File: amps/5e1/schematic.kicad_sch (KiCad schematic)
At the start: 26 parts, among them T1 SE 5k:8

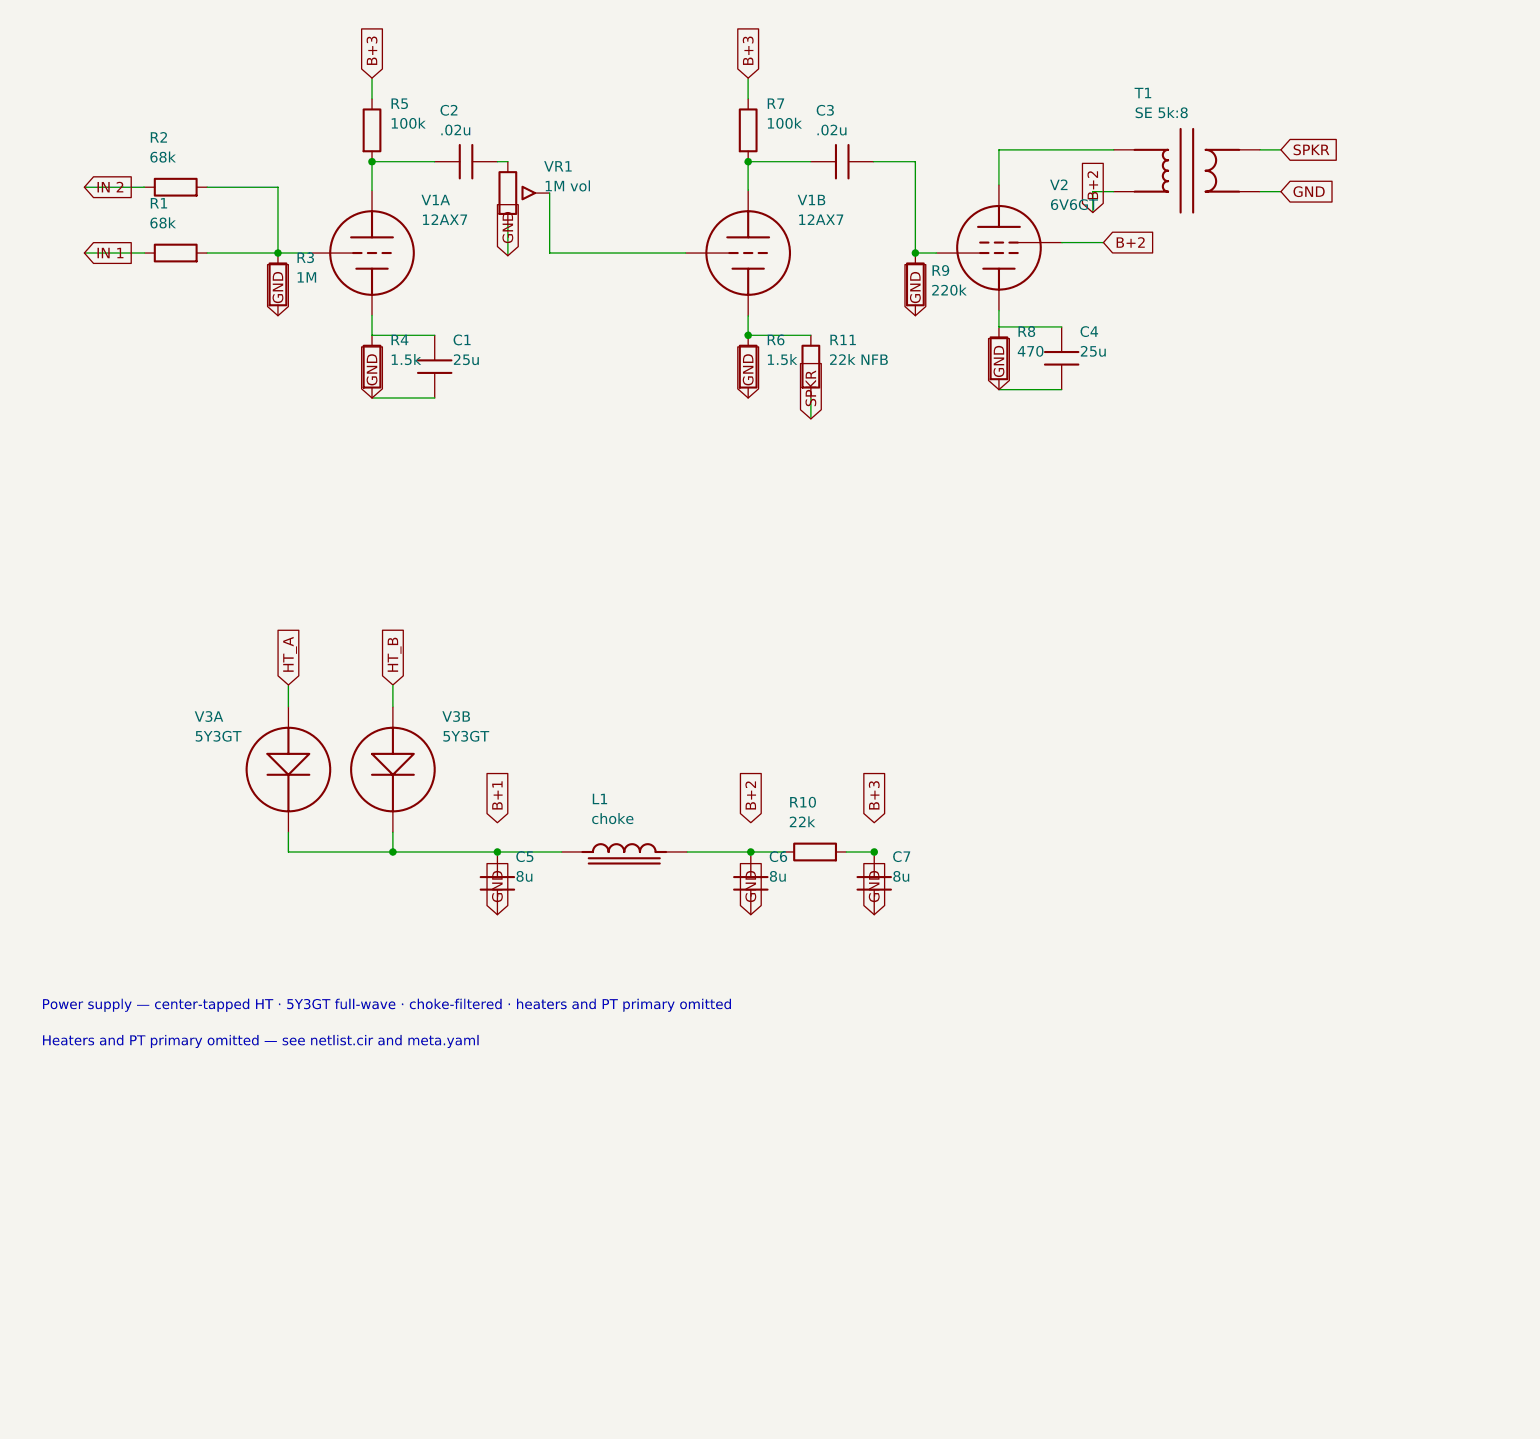
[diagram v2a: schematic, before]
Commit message: Fix: rotated global labels lettered their net names outside the flag
Every global label this pipeline emitted carried (justify left) regardless of
rotation. KiCanvas — like KiCad — draws label text horizontally at 0/180 and
vertically at 90/270 and reads WHICH SIDE of the anchor it letters on from the
justification, so at 180 and 270 the name printed outside an empty flag
outline, struck through by the very wire it names: 219 labels at 180 deg
(including the input-jack flags at top-left of nearly every sheet, the first
glyphs a visitor reads) and 792 GND/rail flags at 270 whose names squeezed at
the flag mouth instead of lettering down the body. The library already
compensated rotation for property text (`pa`); this mirrors that logic for
global labels: justify right at 180/270, left at 0/90.

check_schematics gains the geometry clause whose absence let all 1011
instances through a "no lettering through circuitry" pass: it modelled the
flag box but never the label TEXT, so a name rendered on the wrong side was
invisible to it. The gate now proves justification compensates rotation on
every global label.

Two more things this exposed, fixed in the same engine pass:

- Placement now measures with the renderer's own Newstroke advance table
  (extracted from the vendored kicanvas.js) instead of a flat 0.68-em prose
  average that under-read part lettering by a quarter — the mechanism behind
  every "metered clean, printed through its neighbour" incident. The GATE
  deliberately keeps the coarse ruler: re-ruling it with renderer truth was
  tried and red-flagged 28 of 34 sheets over abutments three visual passes
  had already judged sub-visual (the two-rulers note in schematic_lib.py).
- place_captions' escape ladder runs further, because a banner caption
  measured truly is half again wider than the old estimate believed.

All 34 schematics regenerated; full gate suite green.

🤖 Generated with [Claude Code](https://claude.com/claude-code)

Co-Authored-By: Claude Fable 5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
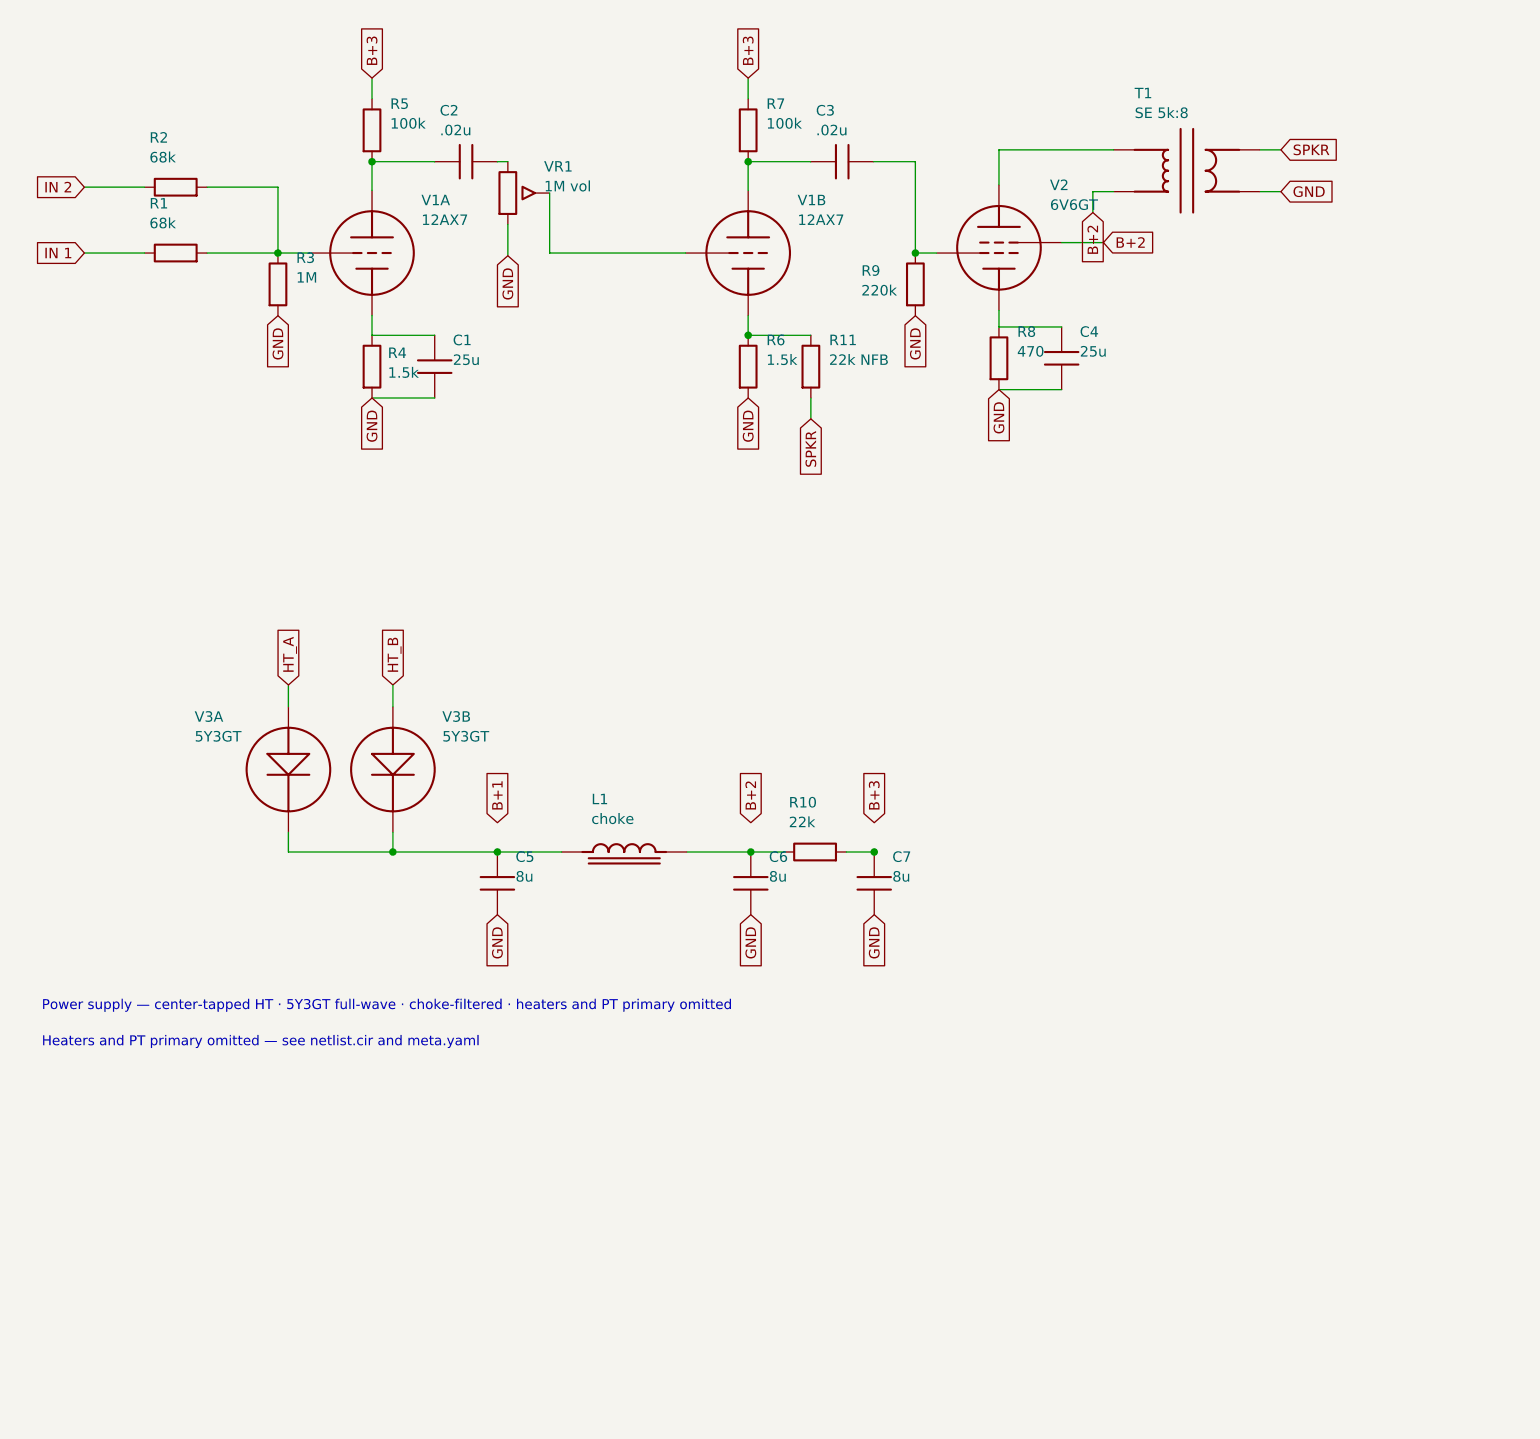
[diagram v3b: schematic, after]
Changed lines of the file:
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@@
     (comment 3 "Values read from: https://el34world.com/charts/Schematics/files/Fender/Fender_champ_5e1.pdf"))
   (global_label "IN 1" (shape input) (at 17.8816 38.278 180)
-    (effects (font (size 1.27 1.27)) (justify left)))
+    (effects (font (size 1.27 1.27)) (justify right)))
   (wire (pts (xy 17.8816 38.278) (xy 25.1716 38.278))
     (stroke (width 0) (type default)))
@@
     (stroke (width 0) (type default)))
   (global_label "IN 2" (shape input) (at 17.8816 30.278 180)
-    (effects (font (size 1.27 1.27)) (justify left)))
+    (effects (font (size 1.27 1.27)) (justify right)))
   (wire (pts (xy 17.8816 30.278) (xy 25.1716 30.278))
     (stroke (width 0) (type default)))
@@
     (property "Value" "1M" (at 43.6116 41.288 0) (effects (font (size 1.27 1.27)) (justify left))))
   (global_label "GND" (shape input) (at 41.4116 45.898 270)
-    (effects (font (size 1.27 1.27)) (justify left)))
+    (effects (font (size 1.27 1.27)) (justify right)))
   (wire (pts (xy 41.4116 38.278) (xy 45.2216 38.278))
     (stroke (width 0) (type default)))
@@
   (symbol (lib_id "cx:R") (at 52.8416 52.088 0) (unit 1)
     (in_bom yes) (on_board yes)
-    (property "Reference" "R4" (at 55.0416 48.888 0) (effects (font (size 1.27 1.27)) (justify left)))
-    (property "Value" "1.5k" (at 55.0416 51.288 0) (effects (font (size 1.27 1.27)) (justify left))))
+    (property "Reference" "R4" (at 54.7576 50.448 0) (effects (font (size 1.27 1.27)) (justify left)))
+    (property "Value" "1.5k" (at 54.7576 52.848 0) (effects (font (size 1.27 1.27)) (justify left))))
   (symbol (lib_id "cx:C") (at 60.4616 52.088 0) (unit 1)
     (in_bom yes) (on_board yes)
@@
     (stroke (width 0) (type default)))
   (global_label "GND" (shape input) (at 52.8416 55.898 270)
-    (effects (font (size 1.27 1.27)) (justify left)))
+    (effects (font (size 1.27 1.27)) (justify right)))
   (wire (pts (xy 52.8416 30.658) (xy 52.8416 27.178))
     (stroke (width 0) (type default)))
@@
     (stroke (width 0) (type default)))
   (global_label "GND" (shape input) (at 69.3516 38.608 270)
-    (effects (font (size 1.27 1.27)) (justify left)))
+    (effects (font (size 1.27 1.27)) (justify right)))
   (wire (pts (xy 74.4316 30.988) (xy 74.4316 38.278))
     (stroke (width 0) (type default)))
@@
     (property "Value" "1.5k" (at 100.762 51.288 0) (effects (font (size 1.27 1.27)) (justify left))))
   (global_label "GND" (shape input) (at 98.5616 55.898 270)
-    (effects (font (size 1.27 1.27)) (justify left)))
+    (effects (font (size 1.27 1.27)) (justify right)))
   (wire (pts (xy 98.5616 48.278) (xy 106.182 48.278))
     (stroke (width 0) (type default)))
@@
     (stroke (width 0) (type default)))
   (global_label "SPKR" (shape input) (at 106.182 58.438 270)
-    (effects (font (size 1.27 1.27)) (justify left)))
+    (effects (font (size 1.27 1.27)) (justify right)))
   (wire (pts (xy 98.5616 30.658) (xy 98.5616 27.178))
     (stroke (width 0) (type default)))
@@
   (symbol (lib_id "cx:R") (at 118.882 42.088 0) (unit 1)
     (in_bom yes) (on_board yes)
-    (property "Reference" "R9" (at 120.798 40.448 0) (effects (font (size 1.27 1.27)) (justify left)))
-    (property "Value" "220k" (at 120.798 42.848 0) (effects (font (size 1.27 1.27)) (justify left))))
+    (property "Reference" "R9" (at 112.31 40.448 0) (effects (font (size 1.27 1.27)) (justify left)))
+    (property "Value" "220k" (at 112.31 42.848 0) (effects (font (size 1.27 1.27)) (justify left))))
   (global_label "GND" (shape input) (at 118.882 45.898 270)
-    (effects (font (size 1.27 1.27)) (justify left)))
+    (effects (font (size 1.27 1.27)) (justify right)))
   (wire (pts (xy 118.882 38.278) (xy 121.422 38.278))
     (stroke (width 0) (type default)))
@@
     (stroke (width 0) (type default)))
   (global_label "GND" (shape input) (at 129.042 54.883 270)
-    (effects (font (size 1.27 1.27)) (justify left)))
+    (effects (font (size 1.27 1.27)) (justify right)))
   (symbol (lib_id "cx:OT_SE") (at 151.882 28.278 0) (unit 1)
     (in_bom yes) (on_board yes)
@@
     (stroke (width 0) (type default)))
   (global_label "B+2" (shape input) (at 140.452 33.358 270)
-    (effects (font (size 1.27 1.27)) (justify left)))
+    (effects (font (size 1.27 1.27)) (justify right)))
   (wire (pts (xy 160.772 25.738) (xy 163.312 25.738))
     (stroke (width 0) (type default)))
@@
     (property "Value" "8u" (at 70.2816 114.088 0) (effects (font (size 1.27 1.27)) (justify left))))
   (global_label "GND" (shape input) (at 68.0816 118.698 270)
-    (effects (font (size 1.27 1.27)) (justify left)))
+    (effects (font (size 1.27 1.27)) (justify right)))
   (global_label "B+1" (shape input) (at 68.0816 107.518 90)
     (effects (font (size 1.27 1.27)) (justify left)))
@@
     (property "Value" "8u" (at 101.082 114.088 0) (effects (font (size 1.27 1.27)) (justify left))))
   (global_label "GND" (shape input) (at 98.8816 118.698 270)
-    (effects (font (size 1.27 1.27)) (justify left)))
+    (effects (font (size 1.27 1.27)) (justify right)))
   (global_label "B+2" (shape input) (at 98.8816 107.518 90)
     (effects (font (size 1.27 1.27)) (justify left)))
@@
     (property "Value" "8u" (at 116.082 114.088 0) (effects (font (size 1.27 1.27)) (justify left))))
   (global_label "GND" (shape input) (at 113.882 118.698 270)
-    (effects (font (size 1.27 1.27)) (justify left)))
+    (effects (font (size 1.27 1.27)) (justify right)))
   (global_label "B+3" (shape input) (at 113.882 107.518 90)
     (effects (font (size 1.27 1.27)) (justify left)))

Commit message: Fix: deterministic schematic ids and wires split at every join
- _u() is uuid5 over (amp id, emission order), so a regeneration of an
  unchanged script is byte-identical and a drift gate becomes possible
- write() splits wire segments at symbol pins, wire ends and junction dots,
  so the file connects exactly what the drawing shows under KiCad's
  endpoint-only semantics (270 pins were on a wire's interior; net
  partitions unchanged on all 38 sheets)
- all sheets regenerated; aa864-bassman title block was stale (draft) and
  now matches meta.yaml (verified)

Co-Authored-By: Claude Fable 5.1 <noreply@anthropic.com>
Claude-Session: https://claude.ai/code/session_01KBMfdh37HmCL2iWcBiL5J1
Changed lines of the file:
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@@
   (wire (pts (xy 55.3816 108.678) (xy 55.3816 111.078))
     (stroke (width 0) (type default)))
-  (wire (pts (xy 42.6816 111.078) (xy 68.0816 111.078))
+  (wire (pts (xy 42.6816 111.078) (xy 55.3816 111.078))
+    (stroke (width 0) (type default)))
+  (wire (pts (xy 55.3816 111.078) (xy 68.0816 111.078))
     (stroke (width 0) (type default)))
   (junction (at 55.3816 111.078) (diameter 0) (color 0 0 0 0))

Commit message: Fix: schematic wiring on 5c1, 5e1, 5e4a, 5e5a, 5e6a, 5f4; all six claim equivalence
- 5c1, 5e1: the B+1/B+2/B+3 labels sat 3.56 mm above the filter chain with
  no lead, naming rails the drawing never reached
- 5e4a, 5e5a, 5e6a, 5f4: the 220k grid leak tapped the coupling-cap node;
  the netlist and the factory-derived layouts both return it at the grid
  pin after the 1.5k stopper (coupler -> stopper -> grid, as jtm45 draws
  it); each stopper now lands on the pentode's own grid pin and the leak
  hangs off that junction
- sch_map.yaml schematic_claim: verified on all six -> 37 of 38 sheets are
  hard-gated; 6g5 stays unclaimed (presence-branch DC path is a source
  question, not a declaration)

Co-Authored-By: Claude Fable 5.1 <noreply@anthropic.com>
Claude-Session: https://claude.ai/code/session_01KBMfdh37HmCL2iWcBiL5J1
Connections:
- net B+1: now also C5.1, L1.1, V3A.2 (K), V3B.2 (K)
- net B+2: now also C6.1, L1.2, R10.1
- net B+3: now also C7.1, R10.2
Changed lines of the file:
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@@
   (global_label "GND" (shape input) (at 68.0816 118.698 270)
     (effects (font (size 1.27 1.27)) (justify right)))
+  (wire (pts (xy 68.0816 107.518) (xy 68.0816 111.078))
+    (stroke (width 0) (type default)))
   (global_label "B+1" (shape input) (at 68.0816 107.518 90)
     (effects (font (size 1.27 1.27)) (justify left)))
@@
   (global_label "GND" (shape input) (at 98.8816 118.698 270)
     (effects (font (size 1.27 1.27)) (justify right)))
+  (wire (pts (xy 98.8816 107.518) (xy 98.8816 111.078))
+    (stroke (width 0) (type default)))
   (global_label "B+2" (shape input) (at 98.8816 107.518 90)
     (effects (font (size 1.27 1.27)) (justify left)))
@@
   (global_label "GND" (shape input) (at 113.882 118.698 270)
     (effects (font (size 1.27 1.27)) (justify right)))
+  (wire (pts (xy 113.882 107.518) (xy 113.882 111.078))
+    (stroke (width 0) (type default)))
   (global_label "B+3" (shape input) (at 113.882 107.518 90)
     (effects (font (size 1.27 1.27)) (justify left)))
